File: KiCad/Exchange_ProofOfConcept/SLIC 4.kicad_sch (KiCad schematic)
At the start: 9 parts

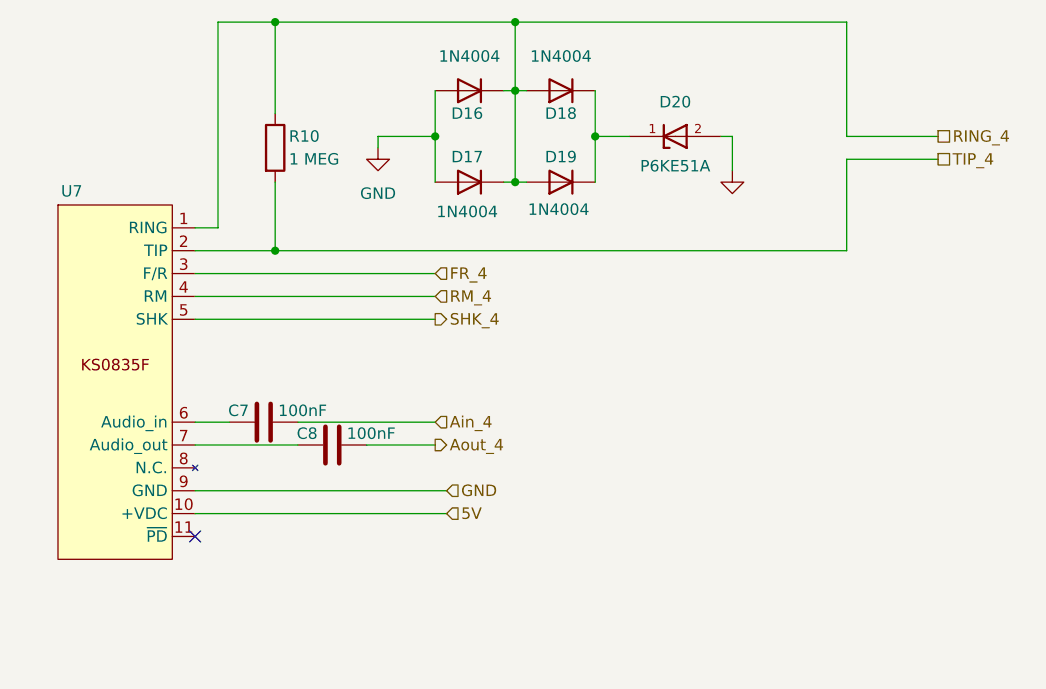
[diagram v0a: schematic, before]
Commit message: deleted:    KiCad/Exchange_ProofOfConcept/Exchange_ProofOfConcept-backups/Exchange_ProofOfConcept-2024-08-28_233227.zip 	deleted:    KiCad/Exchange_ProofOfConcept/Exchange_ProofOfConcept-backups/Exchange_ProofOfConcept-2024-08-28_234504.zip 	deleted:    KiCad/Exchange_ProofOfConcept/Exchange_ProofOfConcept-backups/Exchange_ProofOfConcept-2024-09-04_201626.zip 	deleted:    KiCad/Exchange_ProofOfConcept/Exchange_ProofOfConcept-backups/Exchange_ProofOfConcept-2024-09-04_202659.zip 	deleted:    KiCad/Exchange_ProofOfConcept/Exchange_ProofOfConcept-backups/Exchange_ProofOfConcept-2024-09-04_203703.zip 	deleted:    KiCad/Exchange_ProofOfConcept/Exchange_ProofOfConcept-backups/Exchange_ProofOfConcept-2024-09-04_204710.zip 	deleted:    KiCad/Exchange_ProofOfConcept/Exchange_ProofOfConcept-backups/Exchange_ProofOfConcept-2024-09-04_205754.zip 	deleted:    KiCad/Exchange_ProofOfConcept/Exchange_ProofOfConcept-backups/Exchange_ProofOfConcept-2024-09-05_153643.zip 	deleted:    KiCad/Exchange_ProofOfConcept/Exchange_ProofOfConcept-backups/Exchange_ProofOfConcept-2024-09-05_161017.zip 	deleted:    KiCad/Exchange_ProofOfConcept/Exchange_ProofOfConcept-backups/Exchange_ProofOfConcept-2024-09-05_162441.zip 	deleted:    KiCad/Exchange_ProofOfConcept/Exchange_ProofOfConcept-backups/Exchange_ProofOfConcept-2024-09-05_163641.zip 	deleted:    KiCad/Exchange_ProofOfConcept/Exchange_ProofOfConcept-backups/Exchange_ProofOfConcept-2024-09-06_180233.zip 	deleted:    KiCad/Exchange_ProofOfConcept/Exchange_ProofOfConcept-backups/Exchange_ProofOfConcept-2024-09-06_180943.zip 	deleted:    KiCad/Exchange_ProofOfConcept/Exchange_ProofOfConcept-backups/Exchange_ProofOfConcept-2024-09-06_182256.zip 	deleted:    KiCad/Exchange_ProofOfConcept/Exchange_ProofOfConcept-backups/Exchange_ProofOfConcept-2024-09-06_185314.zip 	deleted:    KiCad/Exchange_ProofOfConcept/Exchange_ProofOfConcept-backups/Exchange_ProofOfConcept-2024-09-06_191143.zip 	deleted:    KiCad/Exchange_ProofOfConcept/Exchange_ProofOfConcep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
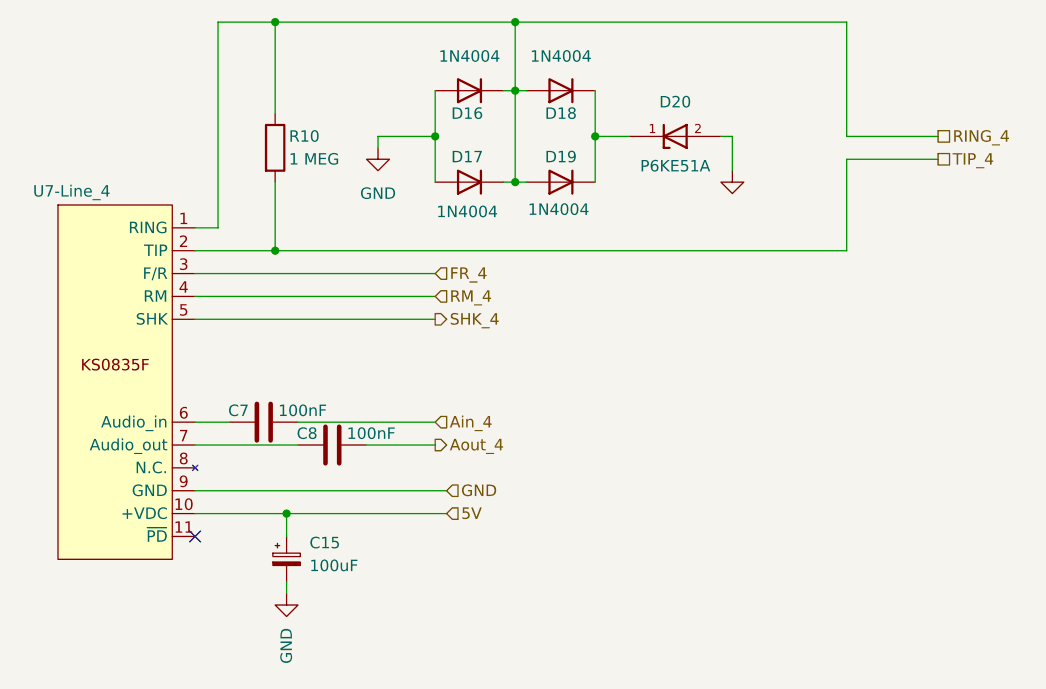
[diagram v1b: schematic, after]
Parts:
- added C15: 100uF, Capacitor_THT:CP_Radial_D5.0mm_P2.00mm, symbol Device:C_Polarized_Small
- renumbered U7 to U7-Line_4
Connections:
- net 5V: now also C15.1
- net GND: now also C15.2
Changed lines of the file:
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@@
+	)
+	(junction
+		(at 62.23 92.71)
+		(diameter 0)
+		(color 0 0 0 0)
 	)
 	(junction
@@
 	(wire
 		(pts
-			(xy 52.07 92.71) (xy 80.01 92.71)
+			(xy 52.07 92.71) (xy 62.23 92.71)
 		)
 		(stroke
@@
 	(wire
 		(pts
+			(xy 62.23 92.71) (xy 80.01 92.71)
+		)
+		(stroke
+			(width 0)
+			(type default)
+		)
+	)
+	(wire
+		(pts
 			(xy 71.12 85.09) (xy 78.74 85.09)
 		)
@@
 	(wire
 		(pts
+			(xy 62.23 100.33) (xy 62.23 101.6)
+		)
+		(stroke
+			(width 0)
+			(type default)
+		)
+	)
+	(wire
+		(pts
 			(xy 96.52 45.72) (xy 96.52 50.8)
 		)
@@
 		(pts
 			(xy 52.07 63.5) (xy 60.96 63.5)
+		)
+		(stroke
+			(width 0)
+			(type default)
+		)
+	)
+	(wire
+		(pts
+			(xy 62.23 95.25) (xy 62.23 92.71)
 		)
 		(stroke
@@
 	)
 	(symbol
+		(lib_id "Device:C_Polarized_Small")
+		(at 62.23 97.79 0)
+		(unit 1)
+		(exclude_from_sim no)
+		(in_bom yes)
+		(on_board yes)
+		(dnp no)
+		(fields_autoplaced yes)
+		(property "Reference" "C15"
+			(at 64.77 95.9738 0)
+			(effects
+				(font
+					(size 1.27 1.27)
+				)
+				(justify left)
+			)
+		)
+		(property "Value" "100uF"
+			(at 64.77 98.5138 0)
+			(effects
+				(font
+					(size 1.27 1.27)
+				)
+				(justify left)
+			)
+		)
+		(property "Footprint" "Capacitor_THT:CP_Radial_D5.0mm_P2.00mm"
+			(at 62.23 97.79 0)
+			(effects
+				(font
+					(size 1.27 1.27)
+				)
+				(hide yes)
+			)
+		)
+		(property "Datasheet" "~"
+			(at 62.23 97.79 0)
+			(effects
+				(font
+					(size 1.27 1.27)
+				)
+				(hide yes)
+			)
+		)
+		(property "Description" "Polarized capacitor, small symbol"
+			(at 62.23 97.79 0)
+			(effects
+				(font
+					(size 1.27 1.27)
+				)
+				(hide yes)
+			)
+		)
+		(pin "1"
+		)
+		(pin "2"
+		)
+		(instances
+			(project "Exchange_ProofOfConcept"
+				(path "/a3aa82f3-37b8-406c-999a-d11513c8e1fa/7068f814-57d4-4b47-8a3f-3945778ea8cb"
+					(reference "C15")
+					(unit 1)
+				)
+			)
+		)
+	)
+	(symbol
 		(lib_id "Diode:1N4004")
 		(at 92.71 45.72 180)
@@
 				(path "/a3aa82f3-37b8-406c-999a-d11513c8e1fa/7068f814-57d4-4b47-8a3f-3945778ea8cb"
 					(reference "D19")
+					(unit 1)
+				)
+			)
+		)
+	)
+	(symbol
+		(lib_id "power:GND")
+		(at 62.23 101.6 0)
+		(unit 1)
+		(exclude_from_sim no)
+		(in_bom yes)
+		(on_board yes)
+		(dnp no)
+		(fields_autoplaced yes)
+		(property "Reference" "#PWR029"
+			(at 62.23 107.95 0)
+			(effects
+				(font
+					(size 1.27 1.27)
+				)
+				(hide yes)
+			)
+		)
+		(property "Value" "GND"
+			(at 62.2301 105.41 90)
+			(effects
+				(font
+					(size 1.27 1.27)
+				)
+				(justify right)
+			)
+		)
+		(property "Footprint" ""
+			(at 62.23 101.6 0)
+			(effects
+				(font
+					(size 1.27 1.27)
+				)
+				(hide yes)
+			)
+		)
+		(property "Datasheet" ""
+			(at 62.23 101.6 0)
+			(effects
+				(font
+					(size 1.27 1.27)
+				)
+				(hide yes)
+			)
+		)
+		(property "Description" "Power symbol creates a global label with name \"GND\" , ground"
+			(at 62.23 101.6 0)
+			(effects
+				(font
+					(size 1.27 1.27)
+				)
+				(hide yes)
+			)
+		)
+		(pin "1"
+		)
+		(instances
+			(project "Exchange_ProofOfConcept"
+				(path "/a3aa82f3-37b8-406c-999a-d11513c8e1fa/7068f814-57d4-4b47-8a3f-3945778ea8cb"
+					(reference "#PWR029")
 					(unit 1)
 				)
@@
 		(on_board yes)
 		(dnp no)
-		(property "Reference" "U7"
+		(property "Reference" "U7-Line_4"
 			(at 38.354 56.896 0)
 			(effects
@@
 			(project "Exchange_ProofOfConcept"
 				(path "/a3aa82f3-37b8-406c-999a-d11513c8e1fa/7068f814-57d4-4b47-8a3f-3945778ea8cb"
-					(reference "U7")
+					(reference "U7-Line_4")
 					(unit 1)
 				)

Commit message: new file:   KiCad/Exchange_ProofOfConcept/ESP-Unit/ESP-Unit-backups/ESP-Unit-2024-10-22_204833.zip 	new file:   KiCad/Exchange_ProofOfConcept/ESP-Unit/ESP-Unit-backups/ESP-Unit-2024-10-22_205851.zip 	new file:   KiCad/Exchange_ProofOfConcept/ESP-Unit/ESP-Unit-backups/ESP-Unit-2024-10-22_214835.zip 	new file:   KiCad/Exchange_ProofOfConcept/ESP-Unit/ESP-Unit-backups/ESP-Unit-2024-10-31_190638.zip 	new file:   KiCad/Exchange_ProofOfConcept/ESP-Unit/ESP-Unit.kicad_pcb 	new file:   KiCad/Exchange_ProofOfConcept/ESP-Unit/ESP-Unit.kicad_prl 	new file:   KiCad/Exchange_ProofOfConcept/ESP-Unit/ESP-Unit.kicad_pro 	new file:   KiCad/Exchange_ProofOfConcept/ESP-Unit/ESP-Unit.kicad_sch 	new file:   KiCad/Exchange_ProofOfConcept/ESP-Unit/fp-info-cache 	deleted:    KiCad/Exchange_ProofOfConcept/Exchange_ProofOfConcept-backups/Exchange_ProofOfConcept-2024-09-09_193050.zip 	deleted:    KiCad/Exchange_ProofOfConcept/Exchange_ProofOfConcept-backups/Exchange_ProofOfConcept-2024-09-10_220108.zip 	deleted:    KiCad/Exchange_ProofOfConcept/Exchange_ProofOfConcept-backups/Exchange_ProofOfConcept-2024-09-10_232037.zip 	deleted:    KiCad/Exchange_ProofOfConcept/Exchange_ProofOfConcept-backups/Exchange_ProofOfConcept-2024-09-11_034329.zip 	deleted:    KiCad/Exchange_ProofOfConcept/Exchange_ProofOfConcept-backups/Exchange_ProofOfConcept-2024-09-11_195456.zip 	deleted:    KiCad/Exchange_ProofOfConcept/Exchange_ProofOfConcept-backups/Exchange_ProofOfConcept-2024-09-17_174014.zip 	deleted:    KiCad/Exchange_ProofOfConcept/Exchange_ProofOfConcept-backups/Exchange_ProofOfConcept-2024-09-17_181112.zip 	deleted:    KiCad/Exchange_ProofOfConcept/Exchange_ProofOfConcept-backups/Exchange_ProofOfConcept-2024-09-19_202603.zip 	deleted:    KiCad/Exchange_ProofOfConcept/Exchange_ProofOfConcept-backups/Exchange_ProofOfConcept-2024-09-19_204637.zip 	deleted:    KiCad/Exchange_ProofOfConcept/Exchange_ProofOfConcept-backups/Exchange_ProofOfConcept-2024-09-19_205646.zip 	deleted:    KiCad/Exchange_ProofOfConcep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
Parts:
- R10: footprint Resistor_THT:R_Axial_DIN0204_L3.6mm_D1.6mm_P5.08mm_Horizontal -> Resistor_THT:R_Axial_DIN0207_L6.3mm_D2.5mm_P7.62mm_Horizontal
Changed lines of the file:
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@@
 			)
 		)
-		(property "Footprint" "Resistor_THT:R_Axial_DIN0204_L3.6mm_D1.6mm_P5.08mm_Horizontal"
+		(property "Footprint" "Resistor_THT:R_Axial_DIN0207_L6.3mm_D2.5mm_P7.62mm_Horizontal"
 			(at 59.182 52.07 90)
 			(effects

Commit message: deleted:    KiCad/Exchange_ProofOfConcept/Exchange_ProofOfConcept-backups/Exchange_ProofOfConcept-2024-09-22_005800.zip 	deleted:    KiCad/Exchange_ProofOfConcept/Exchange_ProofOfConcept-backups/Exchange_ProofOfConcept-2024-09-22_010415.zip 	deleted:    KiCad/Exchange_ProofOfConcept/Exchange_ProofOfConcept-backups/Exchange_ProofOfConcept-2024-09-22_093037.zip 	deleted:    KiCad/Exchange_ProofOfConcept/Exchange_ProofOfConcept-backups/Exchange_ProofOfConcept-2024-09-22_093847.zip 	deleted:    KiCad/Exchange_ProofOfConcept/Exchange_ProofOfConcept-backups/Exchange_ProofOfConcept-2024-09-22_094927.zip 	deleted:    KiCad/Exchange_ProofOfConcept/Exchange_ProofOfConcept-backups/Exchange_ProofOfConcept-2024-10-02_184119.zip 	deleted:    KiCad/Exchange_ProofOfConcept/Exchange_ProofOfConcept-backups/Exchange_ProofOfConcept-2024-10-06_223658.zip 	new file:   KiCad/Exchange_ProofOfConcept/Exchange_ProofOfConcept-backups/Exchange_ProofOfConcept-2024-11-20_223020.zip 	new file:   KiCad/Exchange_ProofOfConcept/Exchange_ProofOfConcept-backups/Exchange_ProofOfConcept-2024-11-20_223933.zip 	new file:   KiCad/Exchange_ProofOfConcept/Exchange_ProofOfConcept-backups/Exchange_ProofOfConcept-2024-11-20_224852.zip 	new file:   KiCad/Exchange_ProofOfConcept/Exchange_ProofOfConcept-backups/Exchange_ProofOfConcept-2024-11-20_230009.zip 	new file:   KiCad/Exchange_ProofOfConcept/Exchange_ProofOfConcept-backups/Exchange_ProofOfConcept-2024-11-20_231023.zip 	new file:   KiCad/Exchange_ProofOfConcept/Exchange_ProofOfConcept-backups/Exchange_ProofOfConcept-2024-11-20_231736.zip 	modified:   KiCad/Exchange_ProofOfConcept/Exchange_ProofOfConcept.kicad_pcb 	modified:   KiCad/Exchange_ProofOfConcept/Exchange_ProofOfConcept.kicad_prl 	modified:   KiCad/Exchange_ProofOfConcept/Exchange_ProofOfConcept.kicad_pro 	modified:   KiCad/Exchange_ProofOfConcept/Exchange_ProofOfConcept.kicad_sch 	modified:   KiCad/Exchange_ProofOfConcept/SLIC 1.kicad_sch 	modified:   KiCad/Exchange_ProofOfConcept/SLIC 1_sch.kicad_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
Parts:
- R10: footprint Resistor_THT:R_Axial_DIN0207_L6.3mm_D2.5mm_P7.62mm_Horizontal -> Resistor_THT:R_Axial_DIN0207_L6.3mm_D2.5mm_P2.54mm_Vertical
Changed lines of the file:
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@@
 			)
 		)
-		(property "Footprint" "Resistor_THT:R_Axial_DIN0207_L6.3mm_D2.5mm_P7.62mm_Horizontal"
+		(property "Footprint" "Resistor_THT:R_Axial_DIN0207_L6.3mm_D2.5mm_P2.54mm_Vertical"
 			(at 59.182 52.07 90)
 			(effects
